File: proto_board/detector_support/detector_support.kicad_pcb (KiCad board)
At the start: 4 copper layers, 94 x 99.1 mm, 93 parts, among them J1 Programming Header, J10 Conn_01x06_Female, J11 DET_CONN, J2 DET_CONN_PWR, J3 BATT_1, J4 BATT_2, J5 BATT_3, J6 BATT_4, J7 TEST_CONN, J8 693072010801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

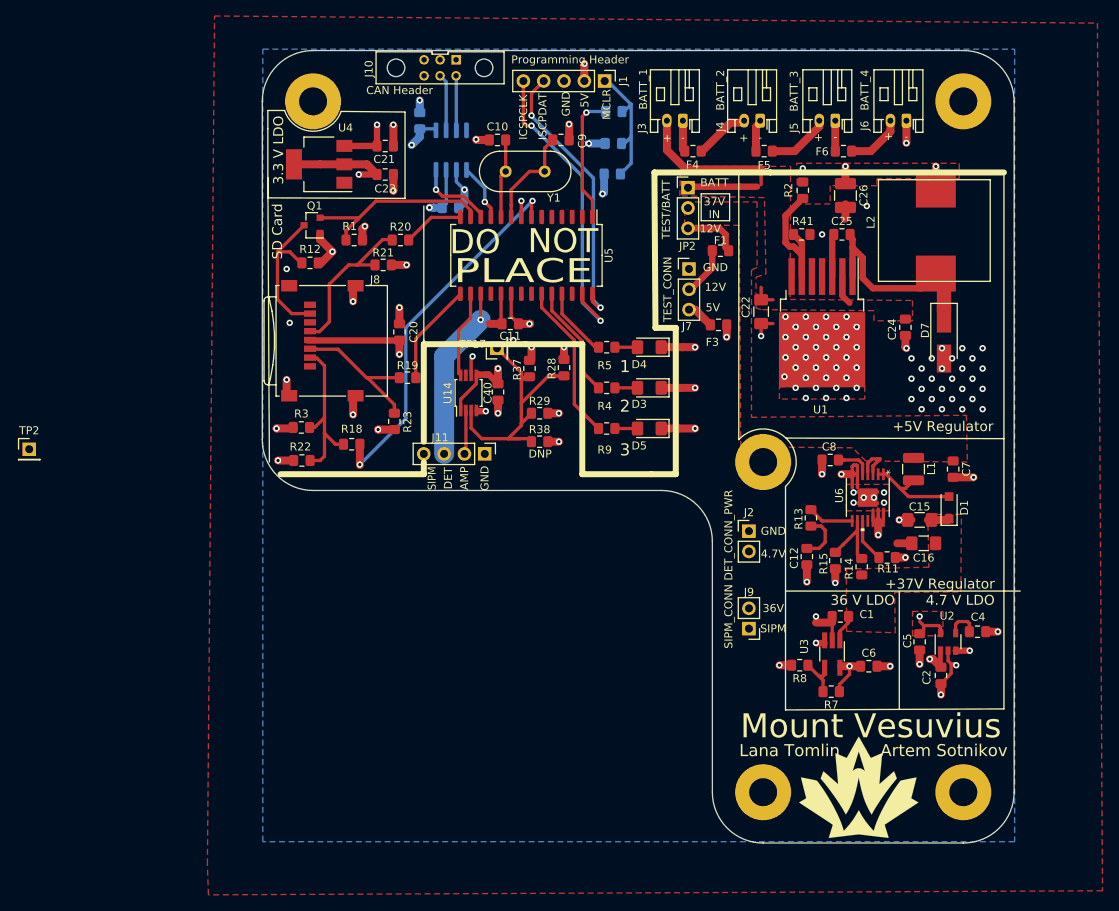
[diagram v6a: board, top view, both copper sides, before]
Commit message: Addressed Zachary's review, re-made gerbers
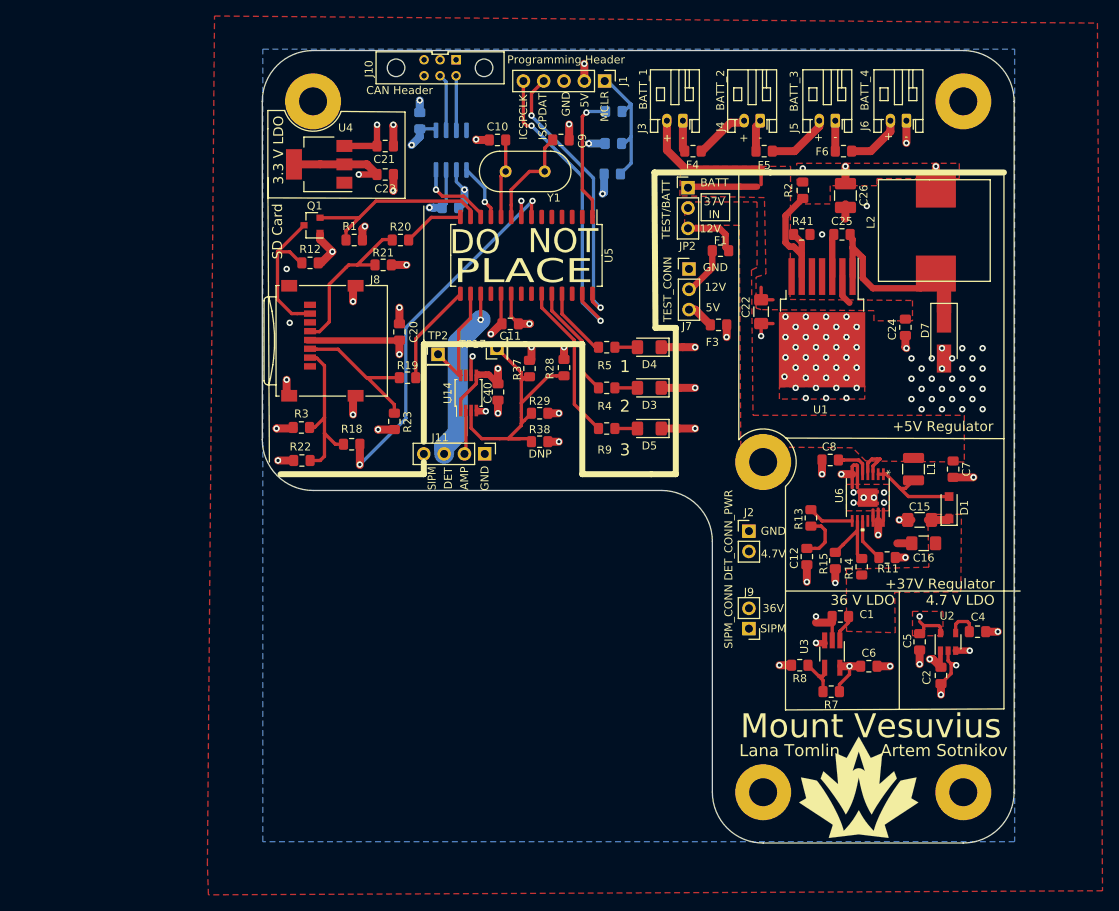
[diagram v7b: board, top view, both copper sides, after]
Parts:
- moved TP2 52.5 mm to (105.8, 86.2)
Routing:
- net /INTERUPT_OUT: track 10.9 -> 14.8 mm

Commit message: Added dates, fixed some small silkscreen issues generated final gerbers GOOD TO FUCKING GO
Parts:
- removed the G*** at (130.9, 97.7)
- added G***: LOGO, Payload2020_custom:volcano2, B.Cu at (130.9, 97.7)
- moved TP17 1.52 mm to (111.6, 85.5)
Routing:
- net Net-(R28-Pad2): track 34.9 -> 37.0 mm
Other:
- board text added: "2021-07-15"
